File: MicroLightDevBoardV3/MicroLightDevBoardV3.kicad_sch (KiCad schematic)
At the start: 32 parts, among them J1 TYPE-C-31-M-12, J2 Conn_01x02_Socket, J3 Conn_01x03_Socket, J4 Conn_01x01_Socket, J5 Conn_01x01_Socket, SW1 SW_Push, U1 USBLC6-2P6, U2 STM32C071GBUx, U3 BQ25180, U4 S-85S1AB33-I6T1U, U5 DF53-2S-0.6H, U7 MC3479

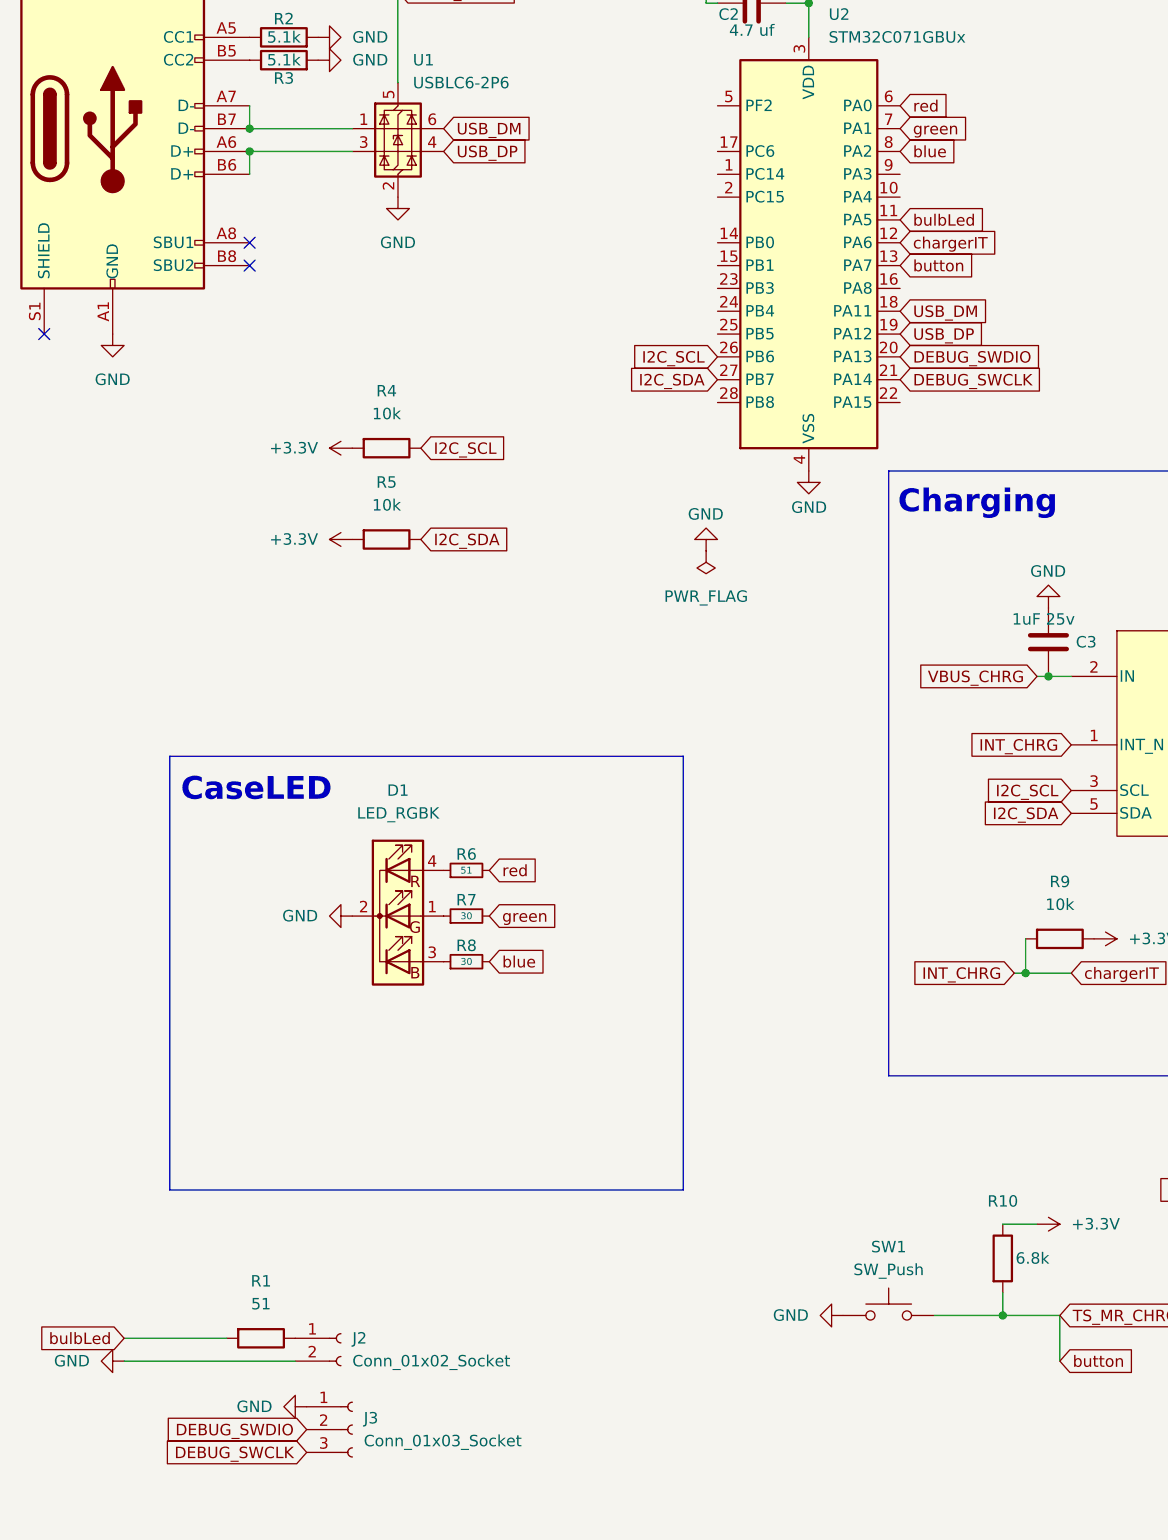
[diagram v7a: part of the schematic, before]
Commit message: added rgb support using timer 3 pins. made rgb/bulb, debug, battery through holes the same diameter
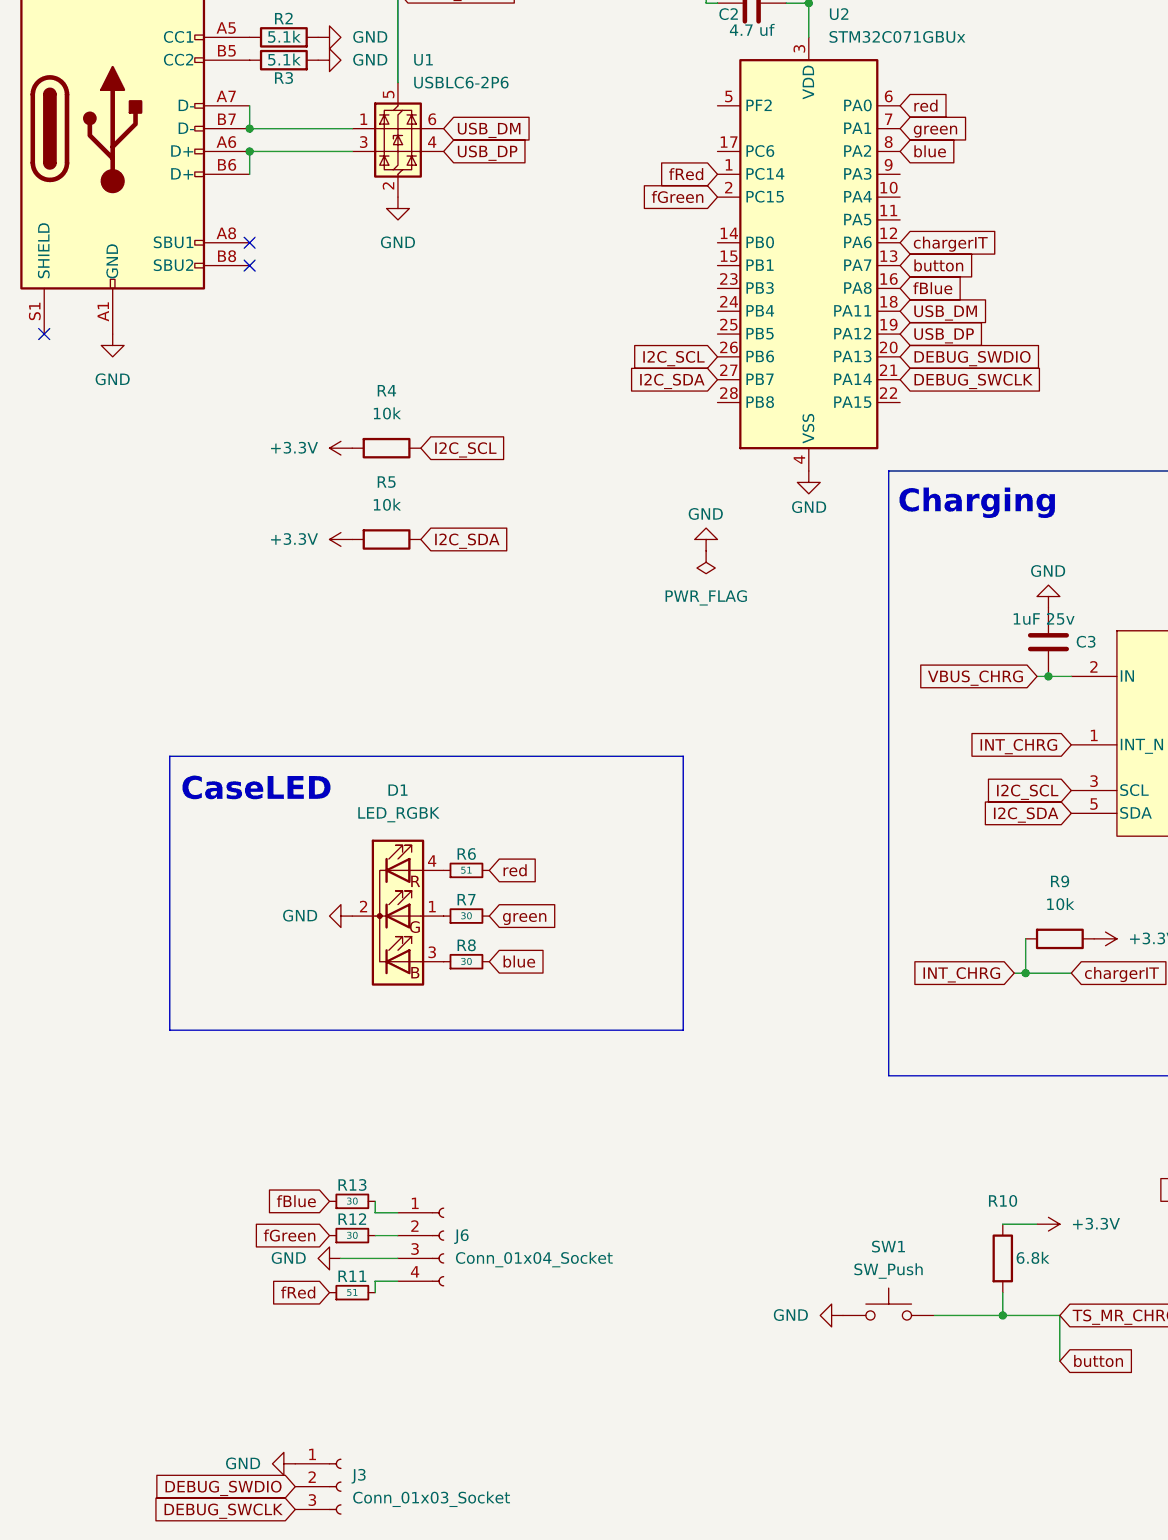
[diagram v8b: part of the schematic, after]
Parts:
- removed J2: Conn_01x02_Socket, Connector_PinSocket_2.54mm:PinSocket_2x01_P2.54mm_Vertical, symbol Connector:Conn_01x02_Socket
- removed R1: 51, Resistor_SMD:R_0402_1005Metric, symbol Device:R
- added J6: Conn_01x04_Socket, Connector_PinSocket_1.27mm:PinSocket_1x04_P1.27mm_Vertical, symbol Connector:Conn_01x04_Socket
- added R11: 51, Resistor_SMD:R_0402_1005Metric, symbol Device:R_Small
- added R12, R13: 30, Resistor_SMD:R_0402_1005Metric, symbol Device:R_Small
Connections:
- net GND: now also J6.3 (Pin_3)
- net fRed: now reaches U2.1 (PC14)
- net fRed: now also R11.1
- net fBlue: now reaches U2.16 (PA8)
- net fBlue: now also R13.1
- net fGreen: now reaches U2.2 (PC15)
- net fGreen: now also R12.1
- net bulbLed: no longer names the net of U2.11 (PA5)
- new net: J6.1 (Pin_1), R13.2
- new net: J6.2 (Pin_2), R12.2
- new net: J6.4 (Pin_4), R11.2
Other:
- moved on the sheet: J3
